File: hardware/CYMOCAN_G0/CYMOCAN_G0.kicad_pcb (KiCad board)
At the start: 2 copper layers, 63.5 x 36.8 mm, 39 parts, among them J1 105450-0101, J2 CAN2 TX|RX, J3 Conn_01x02_Pin, J4 Conn_01x02_Pin, J5 CAN2, J6 DebugEdge_02x05, J7 CAN1 TX|RX, J8 CAN1, SW1 Reset, U1 AP2112K-3.3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

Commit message: Fix DRC issues and Restructure
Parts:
- moved J1 0.76 mm to (106.2, 80.0)
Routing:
- net DEBUG_UART_TX: track 33.1 -> 59.9 mm
- net SWCLK/BOOT0: track 66.2 -> 47.8 mm, vias 2 -> 3
- net CAN1_TX_IND: track 0.00 -> 17.5 mm, vias 0 -> 2
- net USB_DM_ISO: track 46.1 -> 29.4 mm
- net USB_DP: track 31.4 -> 16.0 mm, vias 2 -> 0
- net VCC: track 148.5 -> 133.8 mm
- net SWDIO: track 47.8 -> 36.0 mm
- net USB_DM: track 24.0 -> 32.4 mm
- net Net-(J5-Pin_1): track 22.5 -> 14.6 mm, vias 1 -> 0
- net nRST: track 74.5 -> 67.2 mm
- net CC1: track 18.3 -> 15.0 mm
- net CC2: track 14.2 -> 11.0 mm, vias 2 -> 0
- net GND: track 224.4 -> 221.4 mm, vias 3 -> 0
- net Net-(J3-Pin_1): track 31.3 -> 33.8 mm
- net DEBUG_UART_RX: track 22.2 -> 24.5 mm
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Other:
- board text added: "CYMOCAN-G0"
- board text added: "JLCJLCJLCJLC"
- board text removed: "CYMOCAN_G0"

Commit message: Fix DRC issues
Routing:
- net GND: track 221.4 -> 230.7 mm, vias 0 -> 1
- added copper zone on B.Cu, net GND
- added copper zone on F.Cu, net GND

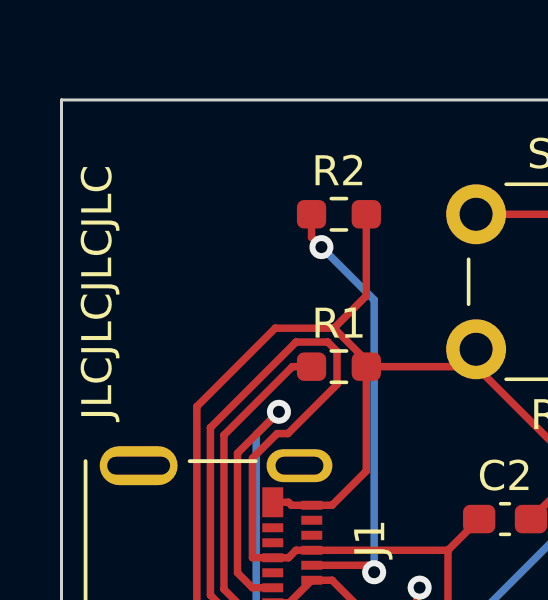
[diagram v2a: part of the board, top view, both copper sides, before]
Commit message: Adjust JLC placeholder
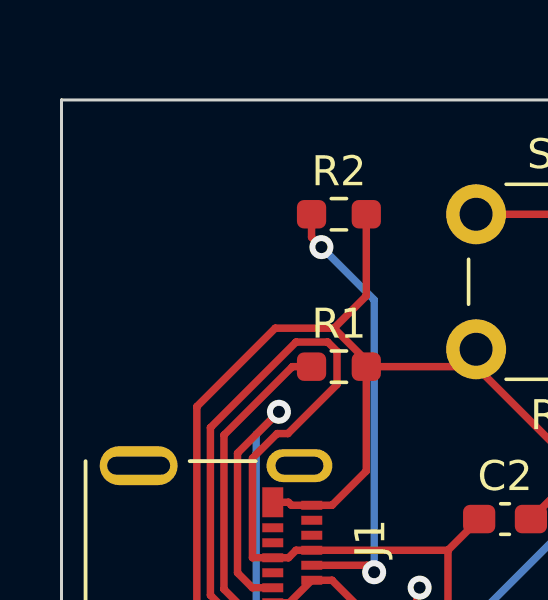
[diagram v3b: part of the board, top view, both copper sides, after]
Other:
- board text added: "JLCJLCJLC"
- board text removed: "JLCJLCJLCJLC"
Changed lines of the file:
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@@
   (gr_line (start 165.1 63.5) (end 101.6 63.5)
     (stroke (width 0.1) (type default)) (layer "Edge.Cuts"))
+  (gr_text "JLCJLCJLC" (at 103.124 72.644 270) (layer "B.SilkS")
+    (effects (font (size 1 1) (thickness 0.15)) (justify left bottom mirror))
+  )
   (gr_text "CYMOCAN-G0" (at 113.792 99.568) (layer "F.SilkS")
     (effects (font (size 1.5 1.5) (thickness 0.3) bold) (justify left bottom))
   )
-  (gr_text "JLCJLCJLCJLC" (at 103.378 74.168 90) (layer "F.SilkS")
-    (effects (font (size 1 1) (thickness 0.15)) (justify left bottom))
-  )
   (segment (start 109.1781 81.26) (end 108.642 81.26) (width 0.25) (layer "F.Cu") (net 1))

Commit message: Fix Led Resistor values
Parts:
- R12: value 1K -> 330
- R13, R6, R7, R8, R9: value 1K -> 220
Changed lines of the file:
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@@
         (effects (font (size 1 1) (thickness 0.15)))
     )
-    (fp_text value "1K" (at 0 1.43) (layer "F.Fab")
+    (fp_text value "220" (at 0 1.43) (layer "F.Fab")
         (effects (font (size 1 1) (thickness 0.15)))
     )
@@
         (effects (font (size 1 1) (thickness 0.15)))
     )
-    (fp_text value "1K" (at 0 1.43) (layer "F.Fab")
+    (fp_text value "330" (at 0 1.43) (layer "F.Fab")
         (effects (font (size 1 1) (thickness 0.15)))
     )
@@
         (effects (font (size 1 1) (thickness 0.15)))
     )
-    (fp_text value "1K" (at 0 1.43 90) (layer "F.Fab")
+    (fp_text value "220" (at 0 1.43 90) (layer "F.Fab")
         (effects (font (size 1 1) (thickness 0.15)))
     )
@@
         (effects (font (size 1 1) (thickness 0.15)))
     )
-    (fp_text value "1K" (at 0 1.43 90) (layer "F.Fab")
+    (fp_text value "220" (at 0 1.43 90) (layer "F.Fab")
         (effects (font (size 1 1) (thickness 0.15)))
     )
@@
         (effects (font (size 1 1) (thickness 0.15)))
     )
-    (fp_text value "1K" (at 0 1.43 90) (layer "F.Fab")
+    (fp_text value "220" (at 0 1.43 90) (layer "F.Fab")
         (effects (font (size 1 1) (thickness 0.15)))
     )
@@
         (effects (font (size 1 1) (thickness 0.15)))
     )
-    (fp_text value "1K" (at 0 1.43 90) (layer "F.Fab")
-        (effects (font (size 1 1) (thickness 0.15)))
-    )
+    (fp_text value "220" (at 0 1.43 90) (layer "F.Fab")
+        (effects (font (size 1 1) (thickness 0.15)))
+    )
